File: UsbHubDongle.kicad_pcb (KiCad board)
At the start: 4 copper layers, 45 x 25 mm, 46 parts, among them J1 USB_C_Receptacle_USB2.0, P1 USB_C_Plug, U1 AP7375-33W5-7, U2 USB2422, Y1 24MHz

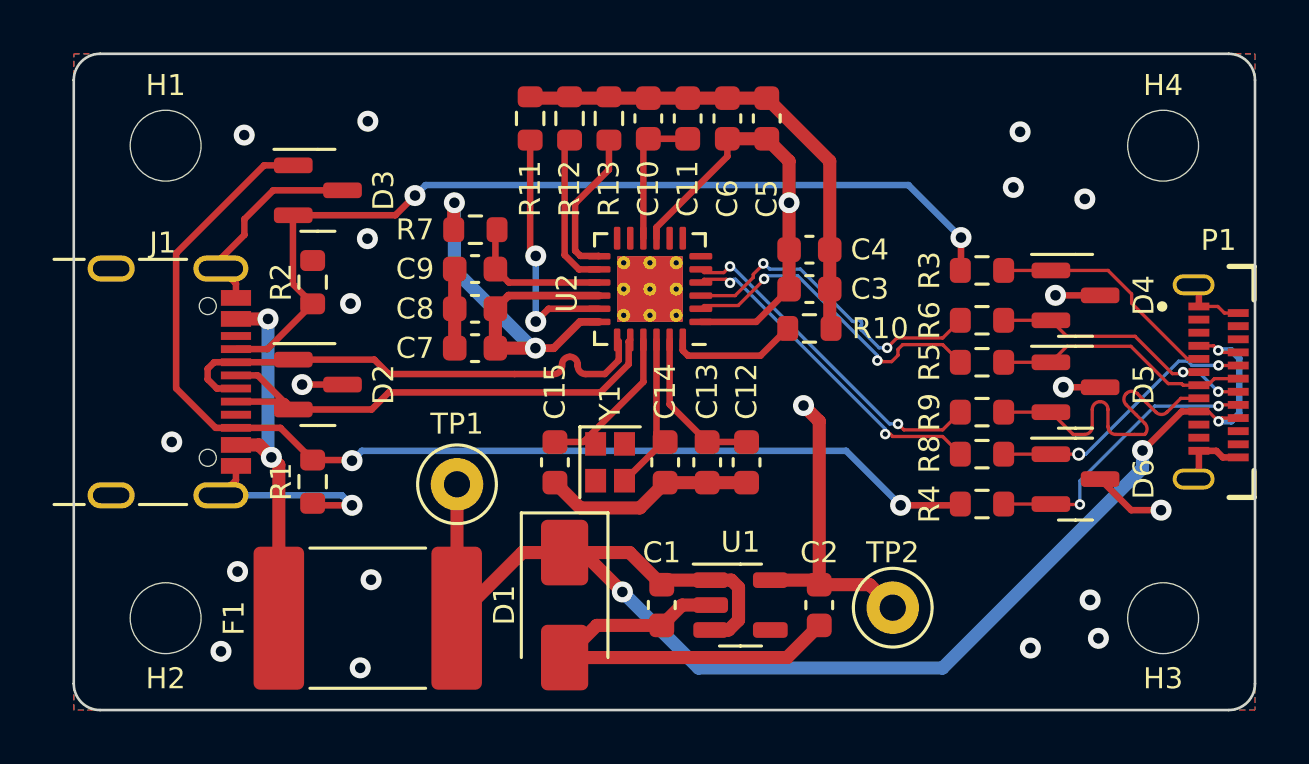
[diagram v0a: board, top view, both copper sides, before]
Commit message: improve the differential pair lines, and increase the min via holes size from 0,2 to 0,3mm
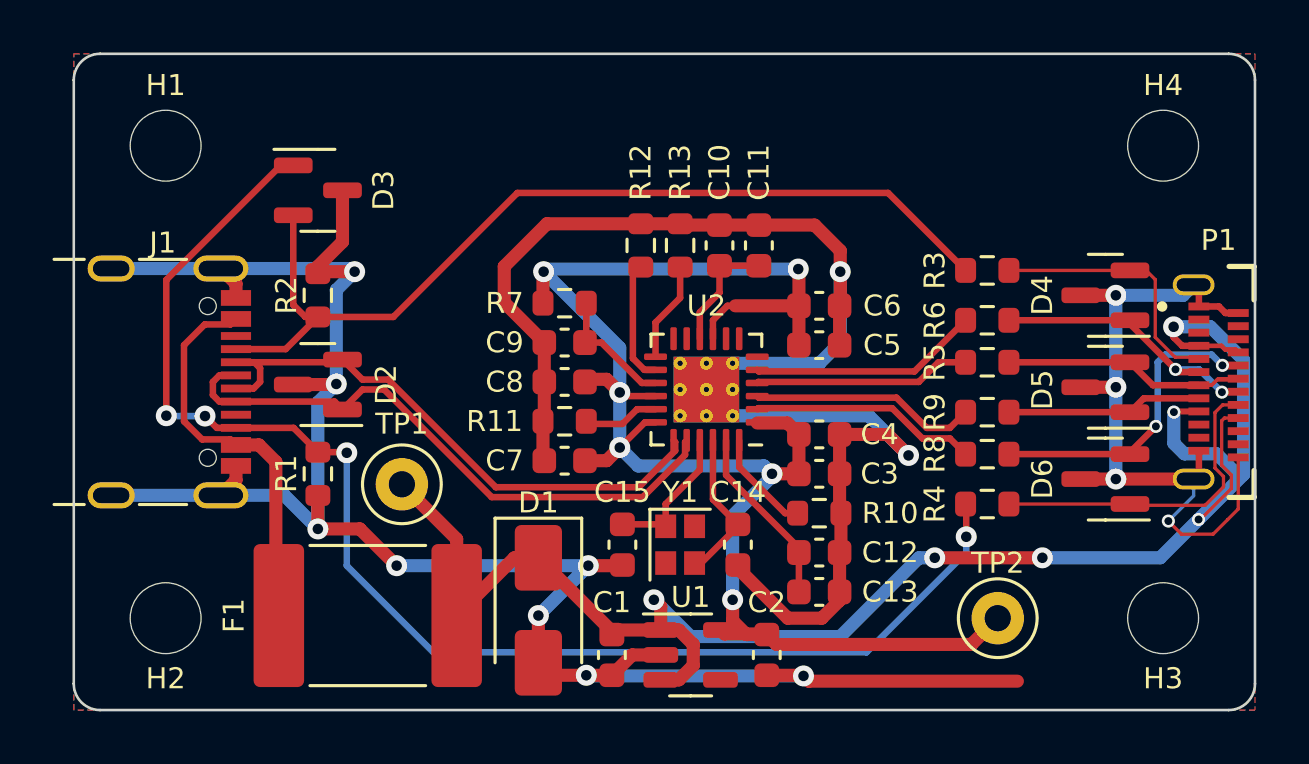
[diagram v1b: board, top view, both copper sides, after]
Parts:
- moved R11 11.6 mm to (118.7, 124.0), turned to 180 degrees
- moved C5 8.87 mm to (128.4, 121.1), turned to 0 degrees
- moved C6 7.95 mm to (128.4, 119.6), turned to 0 degrees
- moved C3 7.05 mm to (128.4, 126.0)
- moved C4 7.05 mm to (128.4, 124.5)
- moved R10 7.05 mm to (128.4, 127.5)
- moved C13 6.53 mm to (128.4, 130.5), turned to 0 degrees
- moved C10 5.55 mm to (124.6, 117.3)
- moved C11 5.55 mm to (126.1, 117.3)
- moved R12 5.55 mm to (121.6, 117.3)
- moved R13 5.55 mm to (123.1, 117.3)
- moved C7 5.48 mm to (118.7, 125.5)
- moved C12 4.41 mm to (128.4, 129.0), turned to 0 degrees
- moved C9 4.41 mm to (118.7, 121.0)
- moved C8 4.41 mm to (118.7, 122.5)
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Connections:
- D2 pad 1: /USB_CONN.D- -> /USB_CONN.D+
- D2 pad 2: /USB_CONN.D+ -> /USB_CONN.D-
- D4 pad 1: /USB.OUT.CC1 -> /SYS.D+
- D4 pad 2: /SYS.D+ -> /USB.OUT.CC1
- D5 pad 1: /SYS.D- -> /GNSS.D+
- D5 pad 2: /GNSS.D+ -> /SYS.D-
- D6 pad 1: /GNSS.D- -> /USB.OUT.CC2
- D6 pad 2: /USB.OUT.CC2 -> /GNSS.D-
- R5 pad 1: /HUB.P1.D- -> /HUB.P2.D-
- R6 pad 1: /HUB.P1.D+ -> /HUB.P2.D+
- R8 pad 1: /HUB.P2.D- -> /HUB.P1.D-
- R9 pad 1: /HUB.P2.D+ -> /HUB.P1.D+
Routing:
- net GND: track 83.5 -> 161.0 mm, vias 20 -> 14
- net +3V3: track 48.1 -> 61.7 mm, vias 4 -> 6
- net VBUS: track 57.7 -> 67.6 mm, vias 4 -> 6
- net /USB_CONN.CC2: track 43.0 -> 52.0 mm, vias 2 -> 4
- net Net-(R11-Pad1): track 9.61 -> 2.91 mm, vias 2 -> 0
- net /GNSS.D+: track 12.9 -> 7.66 mm
- net /HUB.P2.D-: track 12.9 -> 8.26 mm, vias 2 -> 0
- net /HUB.P2.D+: track 12.9 -> 8.77 mm, vias 2 -> 0
- net /HUB.P1.D-: track 12.6 -> 8.68 mm, vias 2 -> 0
- net /HUB.P1.D+: track 12.5 -> 8.69 mm, vias 2 -> 0
- net /USB_CONN.D+: track 19.5 -> 23.0 mm
- net /USB_CONN.D-: track 19.4 -> 22.3 mm
- net Net-(R13-Pad1): track 5.75 -> 3.80 mm
- net /GNSS.D-: track 10.5 -> 12.1 mm
- net /USB.OUT.CC2: track 11.0 -> 12.5 mm, vias 2 -> 0
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- removed copper zone on In1.Cu, net +3V3
- removed copper zone on In2.Cu, net GND
- removed copper zone on In1.Cu, net VBUS
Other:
- copper layers 4 -> 2
- board text added: "0"
- board text added: "0 mm"
- board text added: "0,01 mm"
- board text added: "0,02"
- board text added: "0,035 mm"
- board text added: "0,1270 mm / 0,0000 mm"
- board text added: "0,2000 mm"
- board text added: "1"
- board text added: "1,51 mm"
- board text added: "1,6000 mm"
- board text added: "2"
- board text added: "3,3"
- board text added: "4,5"
- board text added: "45,0000 mm x 25,0000 mm"
- board text added: "B.Cu"
- board text added: "B.Mask"
- board text added: "B.Paste"
- board text added: "B.Silkscreen"
- board text added: "BOARD CHARACTERISTICS"
- board text added: "Board Thickness:"
- board text added: "Board overall dimensions:"
- board text added: "Bottom Silk Screen"
- board text added: "Bottom Solder Mask"
- board text added: "Bottom Solder Paste"
- board text added: "Castellated pads:"
- board text added: "Color"
- board text added: "Copper Finish:"
- board text added: "Copper Layer Count:"
- board text added: "Dielectric 1"
- board text added: "Edge card connectors:"
- board text added: "Epsilon R"
- board text added: "F.Cu"
- board text added: "F.Mask"
- board text added: "F.Paste"
- board text added: "F.Silkscreen"
- board text added: "FR4"
- board text added: "Impedance Control:"
- board text added: "Layer Name"
- board text added: "Loss Tangent"
- board text added: "Material"
- board text added: "Min hole diameter:"
- board text added: "Min track/spacing:"
- board text added: "No"
- board text added: "None"
- board text added: "Not specified"
- board text added: "Plated Board Edge:"
- board text added: "Thickness (mm)"
- board text added: "Top Silk Screen"
- board text added: "Top Solder Mask"
- board text added: "Top Solder Paste"
- board text added: "Type"
- board text added: "copper"
- board text added: "prepreg"
